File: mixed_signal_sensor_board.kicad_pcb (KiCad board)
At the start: 4 copper layers, 0 parts

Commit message: 24V Regulator, Pyro Igniter Circuit
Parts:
- added C1: 4.7uF, Capacitor_SMD:C_0402_1005Metric, F.Cu at (112.0, 26.4)
- added C10: 47pf, Capacitor_SMD:C_0402_1005Metric, F.Cu at (114.9, 32.3)
- added C11: 2.2uF, Capacitor_SMD:C_0402_1005Metric, F.Cu at (114.9, 34.3)
- added C12: 1uF, Capacitor_SMD:C_0402_1005Metric, F.Cu at (114.9, 36.3)
- added C13: 1uF, Capacitor_SMD:C_0402_1005Metric, F.Cu at (117.8, 26.4)
- added C14: 0.1uF, Capacitor_SMD:C_0402_1005Metric, F.Cu at (117.8, 28.4)
- added C15: 1uF, Capacitor_SMD:C_0402_1005Metric, F.Cu at (117.8, 30.4)
- added C16: 1uF, Capacitor_SMD:C_0402_1005Metric, F.Cu at (117.8, 32.3)
- added C17: 1uF, Capacitor_SMD:C_0402_1005Metric, F.Cu at (117.8, 34.3)
- added C18: 10uF, Capacitor_SMD:C_0402_1005Metric, F.Cu at (117.8, 36.3)
- added C19: 0.1uF, Capacitor_SMD:C_0402_1005Metric, F.Cu at (120.6, 26.4)
- added C2: 4.7uF, Capacitor_SMD:C_0402_1005Metric, F.Cu at (112.0, 28.4)
- added C20: 1uF, Capacitor_SMD:C_0402_1005Metric, F.Cu at (120.6, 28.4)
- added C21: 0.22uF, Capacitor_SMD:C_0402_1005Metric, F.Cu at (120.6, 30.4)
- added C22: 0.1uF, Capacitor_SMD:C_0402_1005Metric, F.Cu at (120.6, 32.3)
- added C23: 10nf, Capacitor_SMD:C_0402_1005Metric, F.Cu at (191.5, 84.7)
- added C24: 0.1uF, Capacitor_SMD:C_0402_1005Metric, F.Cu at (191.5, 86.7)
- added C25: 0.1uF, Capacitor_SMD:C_0402_1005Metric, F.Cu at (191.5, 88.6)
- added C26: 10nf, Capacitor_SMD:C_0402_1005Metric, F.Cu at (153.8, 118.0)
- added C27: 0.1uF, Capacitor_SMD:C_0402_1005Metric, F.Cu at (153.8, 119.9)
- added C28: 0.1uF, Capacitor_SMD:C_0402_1005Metric, F.Cu at (153.8, 121.9)
- added C29: 10nf, Capacitor_SMD:C_0402_1005Metric, F.Cu at (153.8, 133.8)
- added C3: 0.47uF, Capacitor_SMD:C_0402_1005Metric, F.Cu at (112.0, 30.4)
- added C30: 0.1uF, Capacitor_SMD:C_0402_1005Metric, F.Cu at (153.8, 135.8)
- added C31: 0.1uF, Capacitor_SMD:C_0402_1005Metric, F.Cu at (153.8, 137.8)
- added C32: 10nf, Capacitor_SMD:C_0402_1005Metric, F.Cu at (173.2, 133.8)
- added C33: 0.1uF, Capacitor_SMD:C_0402_1005Metric, F.Cu at (173.2, 135.8)
- added C34: 0.1uF, Capacitor_SMD:C_0402_1005Metric, F.Cu at (173.2, 137.8)
- added C35: 10nf, Capacitor_SMD:C_0402_1005Metric, F.Cu at (192.6, 118.0)
- added C36: 0.1uF, Capacitor_SMD:C_0402_1005Metric, F.Cu at (192.6, 119.9)
- added C37: 0.1uF, Capacitor_SMD:C_0402_1005Metric, F.Cu at (192.6, 121.9)
- added C38: 10nf, Capacitor_SMD:C_0402_1005Metric, F.Cu at (191.5, 100.6)
- added C39: 0.1uF, Capacitor_SMD:C_0402_1005Metric, F.Cu at (191.5, 102.5)
- added C4: 0.47uF, Capacitor_SMD:C_0402_1005Metric, F.Cu at (112.0, 32.3)
- added C40: 0.1uF, Capacitor_SMD:C_0402_1005Metric, F.Cu at (191.5, 104.5)
- added C41: 10nf, Capacitor_SMD:C_0402_1005Metric, F.Cu at (192.6, 133.8)
- added C42: 0.1uF, Capacitor_SMD:C_0402_1005Metric, F.Cu at (192.6, 135.8)
- added C43: 0.1uF, Capacitor_SMD:C_0402_1005Metric, F.Cu at (192.6, 137.8)
- added C44: 10nf, Capacitor_SMD:C_0402_1005Metric, F.Cu at (173.2, 118.0)
- added C45: 0.1uF, Capacitor_SMD:C_0402_1005Metric, F.Cu at (173.2, 119.9)
- added C46: 0.1uF, Capacitor_SMD:C_0402_1005Metric, F.Cu at (173.2, 121.9)
- added C47: 0.1uF, Capacitor_SMD:C_0402_1005Metric, F.Cu at (121.9, 39.2)
- added C5: 0.1uF, Capacitor_SMD:C_0402_1005Metric, F.Cu at (112.0, 34.3)
- added C6: 4.7uF, Capacitor_SMD:C_0402_1005Metric, F.Cu at (112.0, 36.3)
- added C7: 10uF, Capacitor_SMD:C_0402_1005Metric, F.Cu at (114.9, 26.4)
- added C8: 10uF, Capacitor_SMD:C_0402_1005Metric, F.Cu at (114.9, 28.4)
- added C9: 2.2uF, Capacitor_SMD:C_0402_1005Metric, F.Cu at (114.9, 30.4)
- added D1: SMLVN6RGB, LED_SMD:LED_ROHM_SMLVN6, F.Cu at (152.5, 103.2)
- added D2: LED, LED_SMD:LED_0402_1005Metric, F.Cu at (166.9, 105.3)
- added FB1: 600Ω@100MHz, Inductor_SMD:L_0402_1005Metric, F.Cu at (112.0, 38.2)
- added J1: Conn_01x02, Connector_JST:JST_XH_B2B-XH-A_1x02_P2.50mm_Vertical, F.Cu at (113.9, 70.8)
- added J10: Conn_01x04, Connector_JST:JST_XH_S4B-XH-A_1x04_P2.50mm_Horizontal, F.Cu at (118.0, 128.5)
- added J11: Conn_01x04, Connector_JST:JST_XH_S4B-XH-A_1x04_P2.50mm_Horizontal, F.Cu at (118.0, 142.5)
- added J12: USB_C_Receptacle_USB2.0_16P, Connector_USB:USB_C_Receptacle_GCT_USB4105-xx-A_16P_TopMnt_Horizontal, F.Cu at (176.1, 47.8)
- added J13: Conn_01x04, Connector_JST:JST_XH_B4B-XH-A_1x04_P2.50mm_Vertical, F.Cu at (204.9, 68.8)
- added J14: Conn_01x03, Connector_JST:JST_XH_B3B-XH-A_1x03_P2.50mm_Vertical, F.Cu at (201.9, 130.2)
- added J15: Conn_01x03, Connector_JST:JST_XH_B3B-XH-A_1x03_P2.50mm_Vertical, F.Cu at (198.4, 79.1)
- added J16: Conn_01x03, Connector_JST:JST_XH_B3B-XH-A_1x03_P2.50mm_Vertical, F.Cu at (199.5, 140.3)
- added J17: Conn_01x03, Connector_JST:JST_XH_B3B-XH-A_1x03_P2.50mm_Vertical, F.Cu at (198.4, 98.7)
- added J18: PYRO, Connector_JST:JST_XH_B2B-XH-A_1x02_P2.50mm_Vertical, F.Cu at (230.4, 106.4)
- added J19: PYRO, Connector_JST:JST_XH_B2B-XH-A_1x02_P2.50mm_Vertical, F.Cu at (219.0, 116.2)
- added J2: Conn_01x04, Connector_JST:JST_XH_B4B-XH-A_1x04_P2.50mm_Vertical, F.Cu at (198.4, 88.9)
- added J20: PYRO, Connector_JST:JST_XH_B2B-XH-A_1x02_P2.50mm_Vertical, F.Cu at (219.0, 106.4)
- added J21: PYRO, Connector_JST:JST_XH_B2B-XH-A_1x02_P2.50mm_Vertical, F.Cu at (230.4, 116.2)
- added J3: Conn_01x06, Connector_JST:JST_XH_B6B-XH-A_1x06_P2.50mm_Vertical, F.Cu at (155.9, 159.2)
- added J4: Conn_01x04, Connector_JST:JST_XH_S4B-XH-A_1x04_P2.50mm_Horizontal, F.Cu at (86.4, 92.8)
- added J5: Conn_01x04, Connector_JST:JST_XH_S4B-XH-A_1x04_P2.50mm_Horizontal, F.Cu at (86.4, 107.0)
- added J6: Conn_01x04, Connector_JST:JST_XH_S4B-XH-A_1x04_P2.50mm_Horizontal, F.Cu at (86.4, 121.5)
- added J7: Conn_01x04, Connector_JST:JST_XH_S4B-XH-A_1x04_P2.50mm_Horizontal, F.Cu at (86.4, 136.0)
- added J8: Conn_01x04, Connector_JST:JST_XH_S4B-XH-A_1x04_P2.50mm_Horizontal, F.Cu at (118.5, 99.5)
- added J9: Conn_01x04, Connector_JST:JST_XH_S4B-XH-A_1x04_P2.50mm_Horizontal, F.Cu at (118.0, 114.0)
- added R1: 10K, Resistor_SMD:R_0402_1005Metric, F.Cu at (112.0, 40.2)
- added R10: 120R, Resistor_SMD:R_0402_1005Metric, F.Cu at (117.9, 38.2)
- added R11: 4K7, Resistor_SMD:R_0402_1005Metric, F.Cu at (117.9, 40.2)
- added R12: 4K7, Resistor_SMD:R_0402_1005Metric, F.Cu at (117.9, 42.2)
- added R13: 120R, Resistor_SMD:R_0402_1005Metric, F.Cu at (117.9, 44.2)
- added R14: 1MΩ, Resistor_SMD:R_0402_1005Metric, F.Cu at (191.5, 76.7)
- added R15: 1MΩ, Resistor_SMD:R_0402_1005Metric, F.Cu at (191.5, 78.7)
- added R16: 10K, Resistor_SMD:R_0402_1005Metric, F.Cu at (191.5, 80.7)
- added R17: 10K, Resistor_SMD:R_0402_1005Metric, F.Cu at (191.5, 82.7)
- added R18: 1MΩ, Resistor_SMD:R_0402_1005Metric, F.Cu at (153.8, 110.0)
- added R19: 1MΩ, Resistor_SMD:R_0402_1005Metric, F.Cu at (153.8, 112.0)
- added R2: 5K, Resistor_SMD:R_0402_1005Metric, F.Cu at (112.0, 42.2)
- added R20: 10K, Resistor_SMD:R_0402_1005Metric, F.Cu at (153.8, 114.0)
- added R21: 10K, Resistor_SMD:R_0402_1005Metric, F.Cu at (153.8, 116.0)
- added R22: 1MΩ, Resistor_SMD:R_0402_1005Metric, F.Cu at (153.8, 125.9)
- added R23: 1MΩ, Resistor_SMD:R_0402_1005Metric, F.Cu at (153.8, 127.9)
- added R24: 10K, Resistor_SMD:R_0402_1005Metric, F.Cu at (153.8, 129.9)
- added R25: 10K, Resistor_SMD:R_0402_1005Metric, F.Cu at (153.8, 131.9)
- added R26: 1MΩ, Resistor_SMD:R_0402_1005Metric, F.Cu at (173.2, 125.9)
- added R27: 1MΩ, Resistor_SMD:R_0402_1005Metric, F.Cu at (173.2, 127.9)
- added R28: 10K, Resistor_SMD:R_0402_1005Metric, F.Cu at (173.2, 129.9)
- added R29: 10K, Resistor_SMD:R_0402_1005Metric, F.Cu at (173.2, 131.9)
- added R3: 5K, Resistor_SMD:R_0402_1005Metric, F.Cu at (112.0, 44.2)
- added R30: 1MΩ, Resistor_SMD:R_0402_1005Metric, F.Cu at (192.6, 110.0)
- added R31: 1MΩ, Resistor_SMD:R_0402_1005Metric, F.Cu at (192.6, 112.0)
- added R32: 10K, Resistor_SMD:R_0402_1005Metric, F.Cu at (192.6, 114.0)
- added R33: 10K, Resistor_SMD:R_0402_1005Metric, F.Cu at (192.6, 116.0)
- added R34: 1MΩ, Resistor_SMD:R_0402_1005Metric, F.Cu at (191.5, 92.6)
- added R35: 1MΩ, Resistor_SMD:R_0402_1005Metric, F.Cu at (191.5, 94.6)
- added R36: 10K, Resistor_SMD:R_0402_1005Metric, F.Cu at (191.5, 96.6)
- added R37: 10K, Resistor_SMD:R_0402_1005Metric, F.Cu at (191.5, 98.6)
- added R38: 1MΩ, Resistor_SMD:R_0402_1005Metric, F.Cu at (192.6, 125.9)
- added R39: 1MΩ, Resistor_SMD:R_0402_1005Metric, F.Cu at (192.6, 127.9)
- added R4: 10K, Resistor_SMD:R_0402_1005Metric, F.Cu at (112.0, 46.2)
- added R40: 10K, Resistor_SMD:R_0402_1005Metric, F.Cu at (192.6, 129.9)
- added R41: 10K, Resistor_SMD:R_0402_1005Metric, F.Cu at (192.6, 131.9)
- added R42: 1MΩ, Resistor_SMD:R_0402_1005Metric, F.Cu at (173.2, 110.0)
- added R43: 1MΩ, Resistor_SMD:R_0402_1005Metric, F.Cu at (173.2, 112.0)
- added R44: 10K, Resistor_SMD:R_0402_1005Metric, F.Cu at (173.2, 114.0)
- added R45: 10K, Resistor_SMD:R_0402_1005Metric, F.Cu at (173.2, 116.0)
- added R46: 5K1, Resistor_SMD:R_0402_1005Metric, F.Cu at (209.2, 125.9)
- added R47: 5K1, Resistor_SMD:R_0402_1005Metric, F.Cu at (209.2, 127.9)
- added R48: 22R, Resistor_SMD:R_0402_1005Metric, F.Cu at (209.2, 129.9)
- added R49: 22R, Resistor_SMD:R_0402_1005Metric, F.Cu at (209.2, 131.9)
- added R5: 10K, Resistor_SMD:R_0402_1005Metric, F.Cu at (115.0, 38.2)
- added R50: 120R, Resistor_SMD:R_0402_1005Metric, F.Cu at (121.9, 37.2)
- added R51: 10K, Resistor_SMD:R_0402_1005Metric, F.Cu at (231.5, 94.5)
- added R52: 10K, Resistor_SMD:R_0402_1005Metric, F.Cu at (226.6, 98.5)
- added R53: 10K, Resistor_SMD:R_0402_1005Metric, F.Cu at (226.6, 94.5)
- added R54: 10K, Resistor_SMD:R_0402_1005Metric, F.Cu at (231.5, 98.5)
- added R6: 100K, Resistor_SMD:R_0402_1005Metric, F.Cu at (115.0, 40.2)
- added R7: 16K9, Resistor_SMD:R_0402_1005Metric, F.Cu at (115.0, 42.2)
- added R8: 10K, Resistor_SMD:R_0402_1005Metric, F.Cu at (115.0, 44.2)
- added R9: 10K, Resistor_SMD:R_0402_1005Metric, F.Cu at (115.0, 46.2)
- added SW1: SW_Push, Button_Switch_SMD:SW_SPST_PTS810, F.Cu at (156.9, 76.2)
- added SW2: SW_Push, Button_Switch_SMD:SW_SPST_PTS810, F.Cu at (154.9, 84.2)
- added U1: TMP117xxDRV, Package_SON:WSON-6-1EP_2x2mm_P0.65mm_EP1x1.6mm, F.Cu at (157.8, 103.1)
- added U2: LM27762, Package_SON:WSON-12-1EP_3x2mm_P0.5mm_EP1x2.65_ThermalVias, F.Cu at (162.5, 102.9)
- added U3: MagI3C_171013201, MagI3C_171013201:MagI3C_171013201, F.Cu at (167.1, 102.6)
- added U4: TPS7A20xxxDBV, Package_TO_SOT_SMD:SOT-23-5, F.Cu at (135.9, 63.6)
- added U5: TPS7A20xxxDBV, Package_TO_SOT_SMD:SOT-23-5, F.Cu at (135.9, 70.8)
- added U6: ADS131M08xPBS, Package_QFP:TQFP-32_5x5mm_P0.5mm, F.Cu at (154.7, 65.4)
- added U7: STM32L552CEUx, Package_DFN_QFN:QFN-48-1EP_7x7mm_P0.5mm_EP5.6x5.6mm, F.Cu at (174.8, 64.8)
- added U8: TCAN3414DRBR, TCAN3414DRBR:XCVR_TCAN3414DRBR, F.Cu at (187.4, 64.8)
- added Y1: SG-8018CE_8.192M-TJHSA, SG-8018CE_8.9152M-TJHSA0:OSC_SG-8018CE_8.9152M-TJHSA0, F.Cu at (160.9, 57.2)

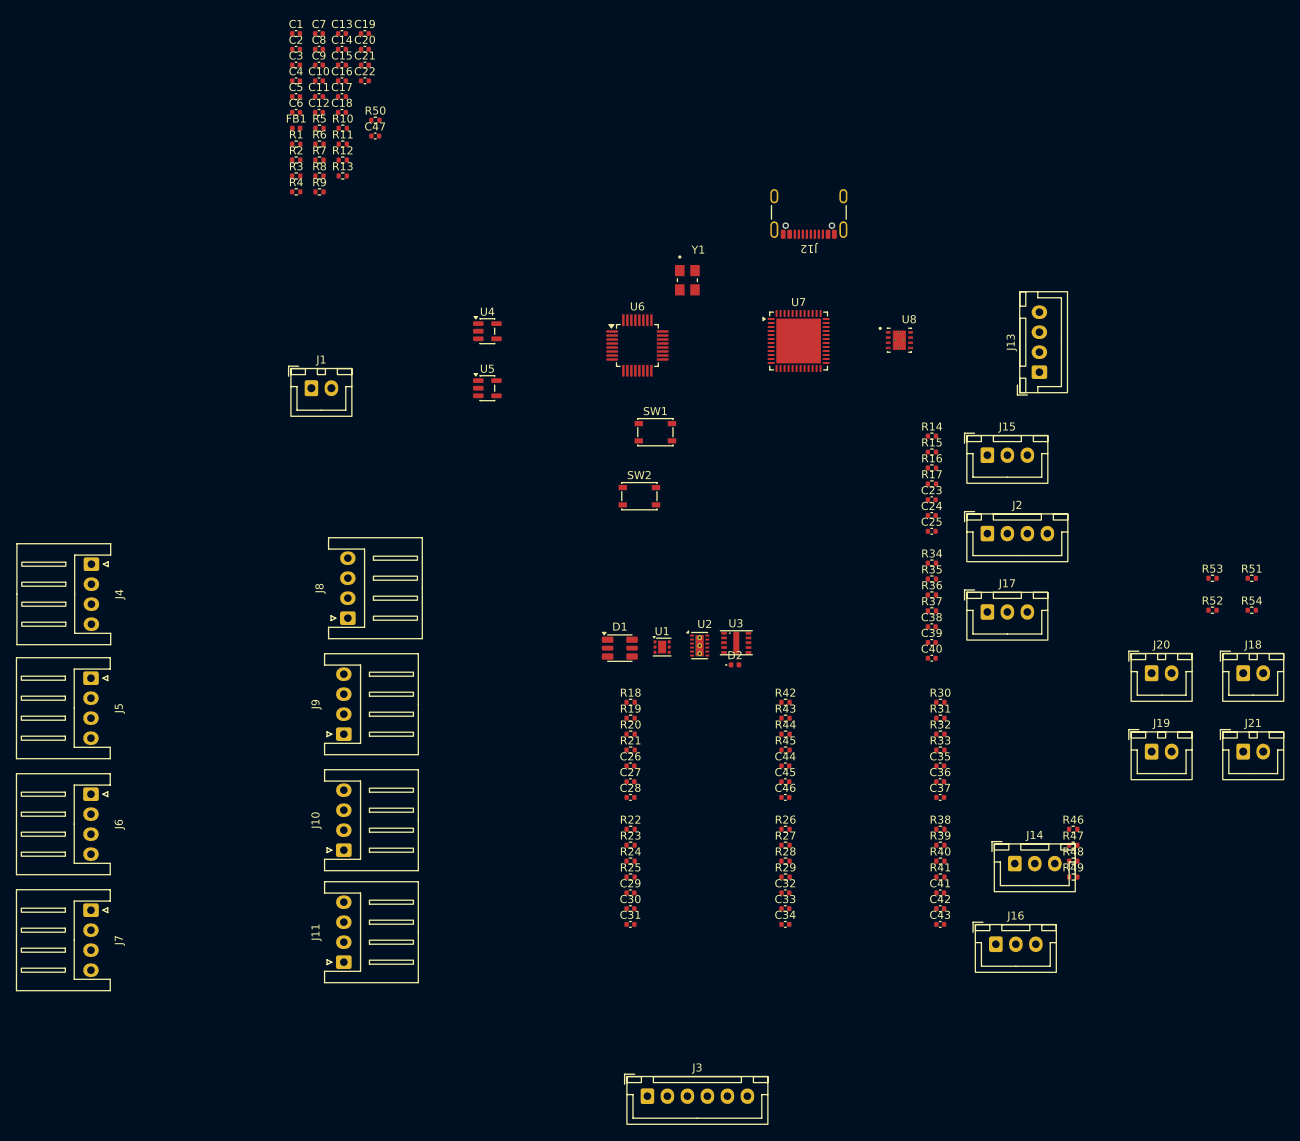
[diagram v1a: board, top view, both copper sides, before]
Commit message: Pyro fault detection, Decoupling Caps STM32, Initial PCB Layout
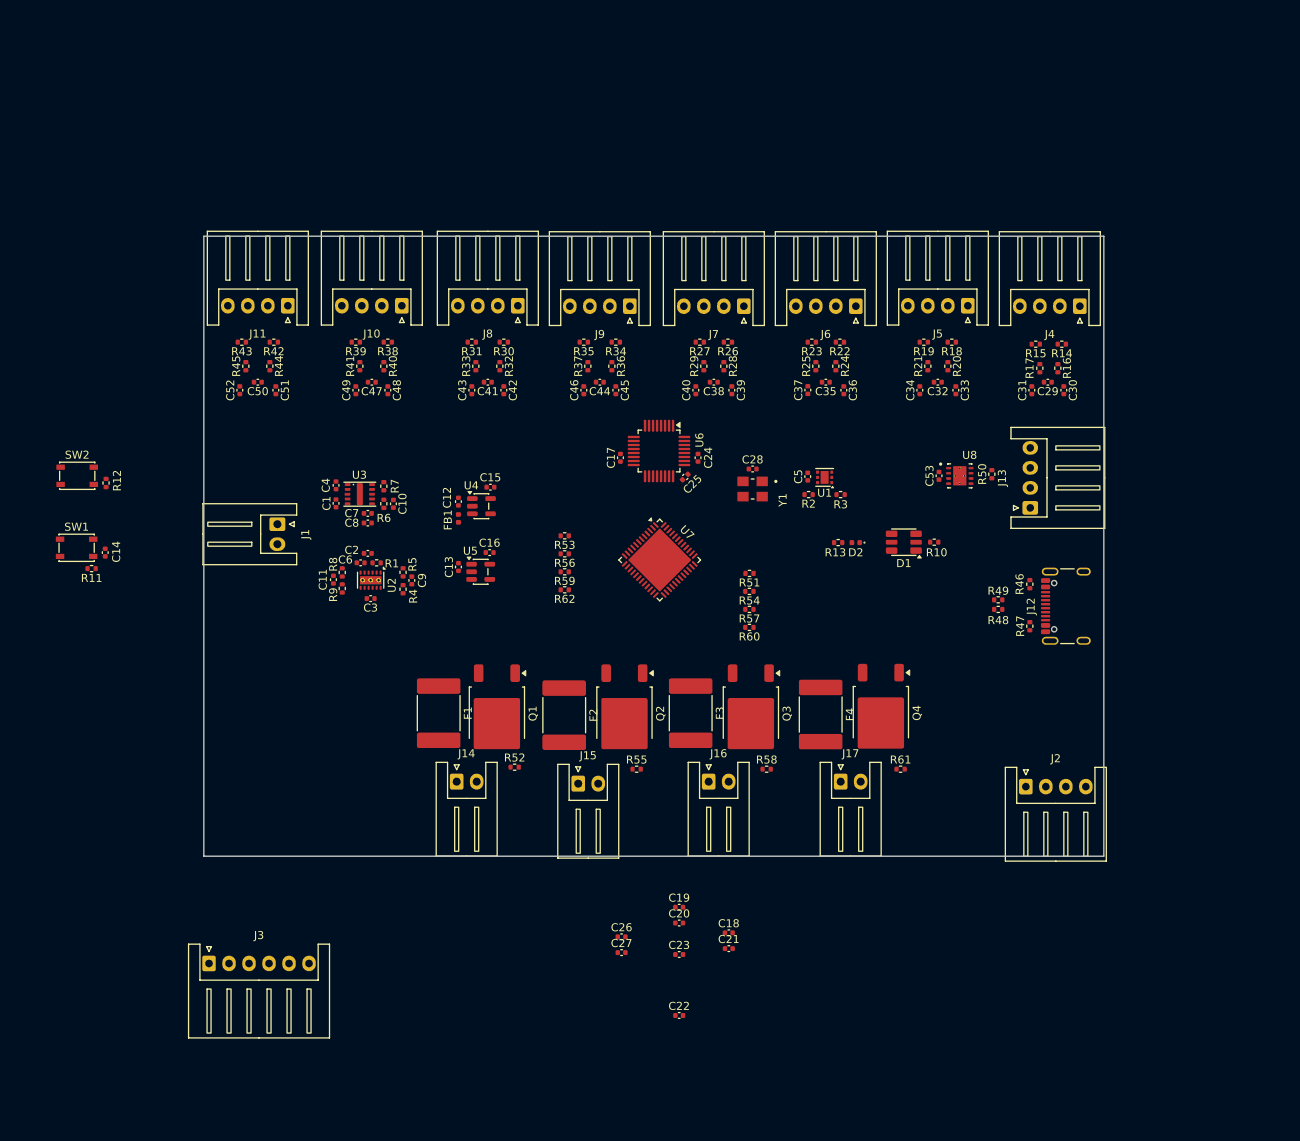
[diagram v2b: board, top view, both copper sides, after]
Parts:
- removed the C46 at (173.2, 121.9)
- removed the C47 at (121.9, 39.2)
- removed the J14 at (201.9, 130.2)
- removed J19, J20, J21: PYRO, Connector_JST:JST_XH_B2B-XH-A_1x02_P2.50mm_Vertical
- added C20: 0.1uF, Capacitor_SMD:C_0402_1005Metric, F.Cu at (159.9, 137.6)
- added C21: 4.7uF, Capacitor_SMD:C_0402_1005Metric, F.Cu at (166.1, 140.8)
- added C22: 4.7uF, Capacitor_SMD:C_0402_1005Metric, F.Cu at (159.9, 149.2)
- added C23: 4.7uF, Capacitor_SMD:C_0402_1005Metric, F.Cu at (159.9, 141.5)
- added C24: 1uF, Capacitor_SMD:C_0402_1005Metric, F.Cu at (162.3, 79.4)
- added C25: 0.22uF, Capacitor_SMD:C_0402_1005Metric, F.Cu at (160.7, 81.8)
- added C28: 0.1uF, Capacitor_SMD:C_0402_1005Metric, F.Cu at (169.1, 80.8)
- added C29: 10nf, Capacitor_SMD:C_0402_1005Metric, F.Cu at (206.0, 70.0)
- added F1: Polyfuse, Fuse:Fuse_2920_7451Metric, F.Cu at (129.9, 111.4)
- added F2: Polyfuse, Fuse:Fuse_2920_7451Metric, F.Cu at (145.6, 111.6)
- added F3: Polyfuse, Fuse:Fuse_2920_7451Metric, F.Cu at (161.4, 111.4)
- added F4: Polyfuse, Fuse:Fuse_2920_7451Metric, F.Cu at (177.6, 111.5)
- added Q1: Q_NMOS_GDS, Package_TO_SOT_SMD:TO-252-2, F.Cu at (137.1, 111.4)
- added Q2: Q_NMOS_GDS, Package_TO_SOT_SMD:TO-252-2, F.Cu at (153.1, 111.4)
- added Q3: Q_NMOS_GDS, Package_TO_SOT_SMD:TO-252-2, F.Cu at (168.9, 111.4)
- added Q4: Q_NMOS_GDS, Package_TO_SOT_SMD:TO-252-2, F.Cu at (185.1, 111.3)
- added R55: 70K, Resistor_SMD:R_0402_1005Metric, F.Cu at (154.6, 118.4)
- added R56: 10K, Resistor_SMD:R_0402_1005Metric, F.Cu at (145.6, 91.5)
- added R57: 10K, Resistor_SMD:R_0402_1005Metric, F.Cu at (168.7, 98.4)
- added R58: 70K, Resistor_SMD:R_0402_1005Metric, F.Cu at (170.9, 118.4)
- added R59: 10K, Resistor_SMD:R_0402_1005Metric, F.Cu at (145.6, 93.7)
- added R60: 10K, Resistor_SMD:R_0402_1005Metric, F.Cu at (168.7, 100.7)
- added R61: 70K, Resistor_SMD:R_0402_1005Metric, F.Cu at (187.6, 118.4)
- added R62: 10K, Resistor_SMD:R_0402_1005Metric, F.Cu at (145.6, 96.0)
- C18: value 10uF -> 0.1uF
- C27: renamed from C21; value 0.22uF -> 10nF
- C31: renamed from C23; value 10nf -> 0.1uF
- C32: renamed from C24; value 0.1uF -> 10nf
- C34: renamed from C26; value 10nf -> 0.1uF
- C35: renamed from C27; value 0.1uF -> 10nf
- C37: renamed from C29; value 10nf -> 0.1uF
- C38: renamed from C30; value 0.1uF -> 10nf
- C40: renamed from C32; value 10nf -> 0.1uF
- C41: renamed from C33; value 0.1uF -> 10nf
- C43: renamed from C35; value 10nf -> 0.1uF
- C44: renamed from C36; value 0.1uF -> 10nf
- C46: renamed from C38; value 10nf -> 0.1uF
- C47: renamed from C39; value 0.1uF -> 10nf
- C49: renamed from C41; value 10nf -> 0.1uF
- C50: renamed from C42; value 0.1uF -> 10nf
- C52: renamed from C44; value 10nf -> 0.1uF
- J1: footprint Connector_JST:JST_XH_B2B-XH-A_1x02_P2.50mm_Vertical -> Connector_JST:JST_XH_S2B-XH-A_1x02_P2.50mm_Horizontal
- J13, J2: footprint Connector_JST:JST_XH_B4B-XH-A_1x04_P2.50mm_Vertical -> Connector_JST:JST_XH_S4B-XH-A_1x04_P2.50mm_Horizontal
- J14: renamed from J18; footprint Connector_JST:JST_XH_B2B-XH-A_1x02_P2.50mm_Vertical -> Connector_JST:JST_XH_S2B-XH-A_1x02_P2.50mm_Horizontal
- J15, J16, J17: value Conn_01x03 -> PYRO; footprint Connector_JST:JST_XH_B3B-XH-A_1x03_P2.50mm_Vertical -> Connector_JST:JST_XH_S2B-XH-A_1x02_P2.50mm_Horizontal
- J3: footprint Connector_JST:JST_XH_B6B-XH-A_1x06_P2.50mm_Vertical -> Connector_JST:JST_XH_S6B-XH-A_1x06_P2.50mm_Horizontal
- R52: value 10K -> 70K
- moved J4 127.7 mm to (210.0, 60.5), turned to 180 degrees
- moved J5 119.1 mm to (196.0, 60.4), turned to 180 degrees
- moved C19 116.1 mm to (159.9, 135.6)
- moved C26 115.5 mm to (152.7, 139.3)
- moved C27 115.5 mm to (152.7, 141.3)
- moved J6 113.4 mm to (182.0, 60.5), turned to 180 degrees
- moved C18 113.4 mm to (166.1, 138.8)
- moved J7 111.2 mm to (168.0, 60.5), turned to 180 degrees
- moved C50 107.7 mm to (107.2, 70.0), turned to 180 degrees
- moved C51 106.6 mm to (109.5, 71.0), turned to -90 degrees
- moved J14 99.2 mm to (132.1, 119.9)
- moved R41 96.7 mm to (120.0, 68.0), turned to 90 degrees
- moved R39 96.4 mm to (119.5, 65.0), turned to 180 degrees
- moved C49 96.4 mm to (119.5, 71.0), turned to 90 degrees
- moved C30 95.5 mm to (208.0, 71.0), turned to -90 degrees
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- renumbered C20 to C26, C22 to C30, C25 to C33, C28 to C36, C31 to C39, C34 to C42, C37 to C45, C40 to C48, C43 to C51, C45 to C53
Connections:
- net /PYRO1 renamed /PYRO1_SIGNAL
- C26 pad 1: +3V3 -> GND
- C26 pad 2: GND -> +3V3A
- C27 pad 1: Net-(U6-CAP) -> GND
- C27 pad 2: GND -> +3V3A
- C30 pad 1: GND -> /SB1/AOUT_P
- C30 pad 2: +3V3 -> GND
- C31 pad 1: /SB1/AOUT_P -> GND
- C32 pad 1: /SB1/AOUT_P -> /SB2/AOUT_P
- C32 pad 2: GND -> /SB2/AOUT_N
- C33 pad 1: GND -> /SB2/AOUT_P
- C33 pad 2: /SB1/AOUT_N -> GND
- C34 pad 1: /SB2/AOUT_P -> GND
- C35 pad 1: /SB2/AOUT_P -> /SB3/AOUT_P
- C35 pad 2: GND -> /SB3/AOUT_N
- C36 pad 1: GND -> /SB3/AOUT_P
- C36 pad 2: /SB2/AOUT_N -> GND
- C37 pad 1: /SB3/AOUT_P -> GND
- C38 pad 1: /SB3/AOUT_P -> /SB4/AOUT_P
- C38 pad 2: GND -> /SB4/AOUT_N
- C39 pad 1: GND -> /SB4/AOUT_P
- C39 pad 2: /SB3/AOUT_N -> GND
- C40 pad 1: /SB4/AOUT_P -> GND
- C41 pad 1: /SB4/AOUT_P -> /SB5/AOUT_P
- C41 pad 2: GND -> /SB5/AOUT_N
- C42 pad 1: GND -> /SB5/AOUT_P
- C42 pad 2: /SB4/AOUT_N -> GND
- C43 pad 1: /SB5/AOUT_P -> GND
- C44 pad 1: /SB5/AOUT_P -> /SB6/AOUT_P
- C44 pad 2: GND -> /SB6/AOUT_N
- C45 pad 1: GND -> /SB6/AOUT_P
- C45 pad 2: /SB5/AOUT_N -> GND
- C46 pad 1: /SB6/AOUT_P -> GND
- C47 pad 1: /SB6/AOUT_P -> /SB7/AOUT_P
- C47 pad 2: GND -> /SB7/AOUT_N
- C48 pad 1: GND -> /SB7/AOUT_P
- C48 pad 2: /SB6/AOUT_N -> GND
- C49 pad 1: /SB7/AOUT_P -> GND
- C50 pad 1: /SB7/AOUT_P -> /SB8/AOUT_P
- C50 pad 2: GND -> /SB8/AOUT_N
- C51 pad 1: GND -> /SB8/AOUT_P
- C51 pad 2: /SB7/AOUT_N -> GND
- C52 pad 1: /SB8/AOUT_P -> GND
- C53 pad 1: /SB8/AOUT_P -> +3V3
- J14 pad 2: Net-(J18-Pin_2) -> Net-(J14-Pin_2)
- J15 pad 1: +24V -> Net-(J15-Pin_1)
- J15 pad 2: /PYRO2 -> Net-(J15-Pin_2)
- J16 pad 1: +24V -> Net-(J16-Pin_1)
- J16 pad 2: /PYRO3 -> Net-(J16-Pin_2)
- J17 pad 1: +24V -> Net-(J17-Pin_1)
- J17 pad 2: /PYRO4 -> Net-(J17-Pin_2)
- R52 pad 1: GND -> /PYRO1_FAULT
- R52 pad 2: /PYRO2 -> Net-(J14-Pin_2)
- R53 pad 1: GND -> /PYRO1_FAULT
- R53 pad 2: /PYRO3 -> GND
- R54 pad 2: /PYRO4 -> /PYRO2_SIGNAL
- U7 pad 10: unconnected-(U7-PA0-Pad10) -> /PYRO1_FAULT
- U7 pad 11: unconnected-(U7-PA1-Pad11) -> /PYRO2_FAULT
- U7 pad 12: unconnected-(U7-PA2-Pad12) -> /PYRO3_FAULT
- U7 pad 13: unconnected-(U7-PA3-Pad13) -> /PYRO4_FAULT
- U7 pad 26: /PYRO2 -> /PYRO2_SIGNAL
- U7 pad 27: /PYRO3 -> /PYRO3_SIGNAL
- U7 pad 28: /PYRO4 -> /PYRO4_SIGNAL
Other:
- board outline added: 112.5 x 77.5 mm

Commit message: Finished first rough initial layout
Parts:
- moved C21 53.0 mm to (159.7, 88.2), turned to 135 degrees
- moved C22 52.9 mm to (163.2, 96.4), turned to 45 degrees
- moved C27 50.7 mm to (152.7, 90.6), turned to -135 degrees
- moved C18 50.5 mm to (159.0, 88.9), turned to 135 degrees
- moved C26 48.0 mm to (153.4, 91.3), turned to -135 degrees
- moved R62 44.8 mm to (189.5, 104.8), turned to 90 degrees
- moved C23 41.7 mm to (155.1, 100.1), turned to -45 degrees
- moved C19 40.0 mm to (162.5, 95.7), turned to 45 degrees
- moved C20 38.5 mm to (155.9, 99.3), turned to -45 degrees
- moved R51 30.8 mm to (139.8, 104.2)
- moved R59 29.8 mm to (173.2, 104.8), turned to 90 degrees
- moved J3 23.2 mm to (103.5, 119.6)
- moved R60 19.4 mm to (187.8, 104.2)
- moved C14 19.3 mm to (104.3, 101.8)
- moved R11 19.3 mm to (102.6, 103.8)
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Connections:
- U7 pad 10: /PYRO1_FAULT -> /ADS_DRDY
- U7 pad 11: /PYRO2_FAULT -> /ADS_SYNC/RESET
- U7 pad 12: /PYRO3_FAULT -> unconnected-(U7-PA2-Pad12)
- U7 pad 13: /PYRO4_FAULT -> unconnected-(U7-PA3-Pad13)
- U7 pad 18: /LEDB -> /PYRO1_SIGNAL
- U7 pad 19: /LEDG -> /PYRO1_FAULT
- U7 pad 20: /LEDR -> /PYRO2_SIGNAL
- U7 pad 21: unconnected-(U7-PB10-Pad21) -> /PYRO2_FAULT
- U7 pad 25: /PYRO1_SIGNAL -> unconnected-(U7-PB12-Pad25)
- U7 pad 26: /PYRO2_SIGNAL -> unconnected-(U7-PB13-Pad26)
- U7 pad 27: /PYRO3_SIGNAL -> unconnected-(U7-PB14-Pad27)
- U7 pad 28: /PYRO4_SIGNAL -> /PYRO3_FAULT
- U7 pad 29: unconnected-(U7-PA8-Pad29) -> /PYRO3_SIGNAL
- U7 pad 30: unconnected-(U7-PA9-Pad30) -> /PYRO4_FAULT
- U7 pad 31: unconnected-(U7-PA10-Pad31) -> /PYRO4_SIGNAL
- U7 pad 39: unconnected-(U7-PB3-Pad39) -> /LEDG
- U7 pad 40: unconnected-(U7-PB4-Pad40) -> /LEDR
- U7 pad 41: unconnected-(U7-PB5-Pad41) -> /LEDB
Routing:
- net (no net): vias 0 -> 4
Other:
- board size 112.5 x 77.5 mm -> 128 x 77.5 mm
- board text added: "3V3"
- board text added: "B.SECZKOWSKI"
- board text added: "BOOT"
- board text added: "CANH"
- board text added: "CANL"
- board text added: "CS"
- board text added: "D.THIEL"
- board text added: "GND"
- board text added: "MISO"
- board text added: "MOSI"
- board text added: "RESET"
- board text added: "SCL"
- board text added: "SCLK"
- board text added: "SDA"
- board text added: "STATUS"
